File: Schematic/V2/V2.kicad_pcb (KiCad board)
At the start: 2 copper layers, 67 x 55 mm, 15 parts, among them J1 OUT1, J2 OUT2, J3 OUT3, J4 OUT4, J5 OUT5, J6 5V ESP, J7 5V LEDS

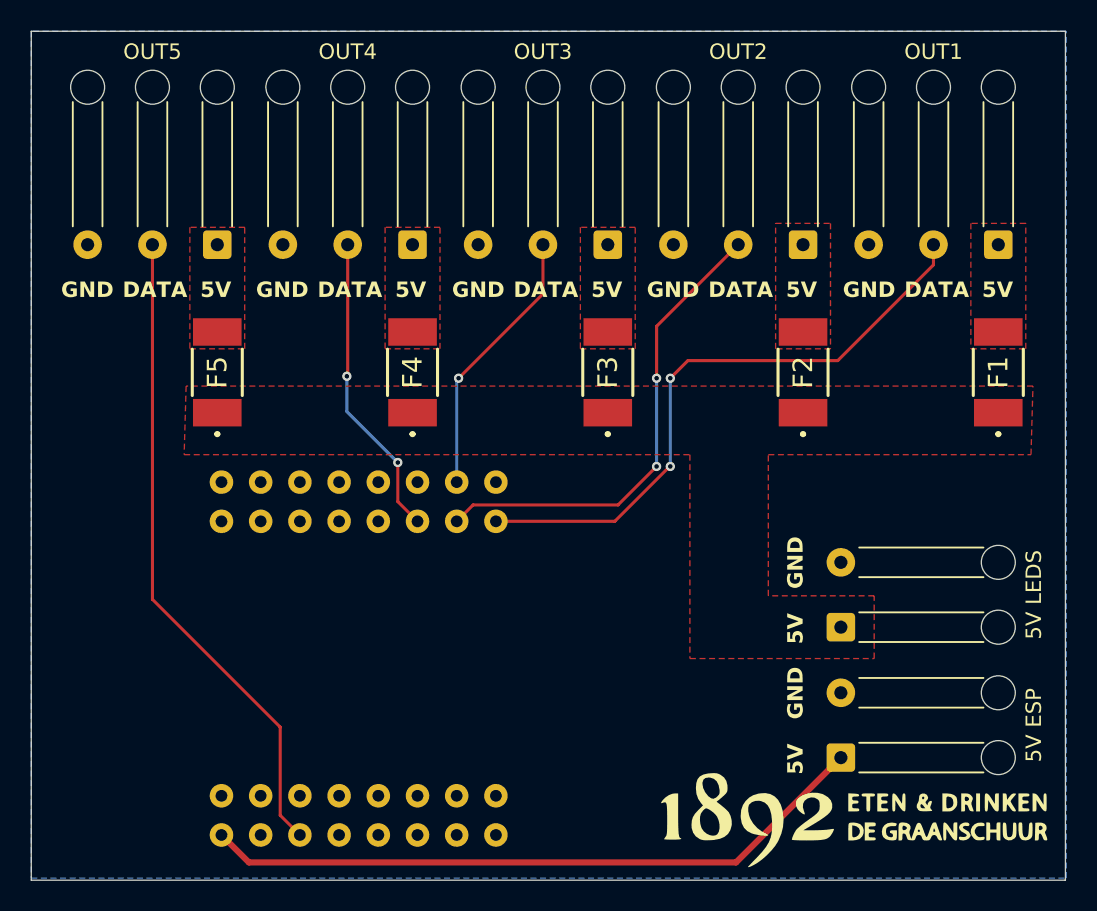
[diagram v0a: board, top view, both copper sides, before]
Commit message: Added support for two 18 AWG wires as 5V input to allow 14A and updated traces as needed.
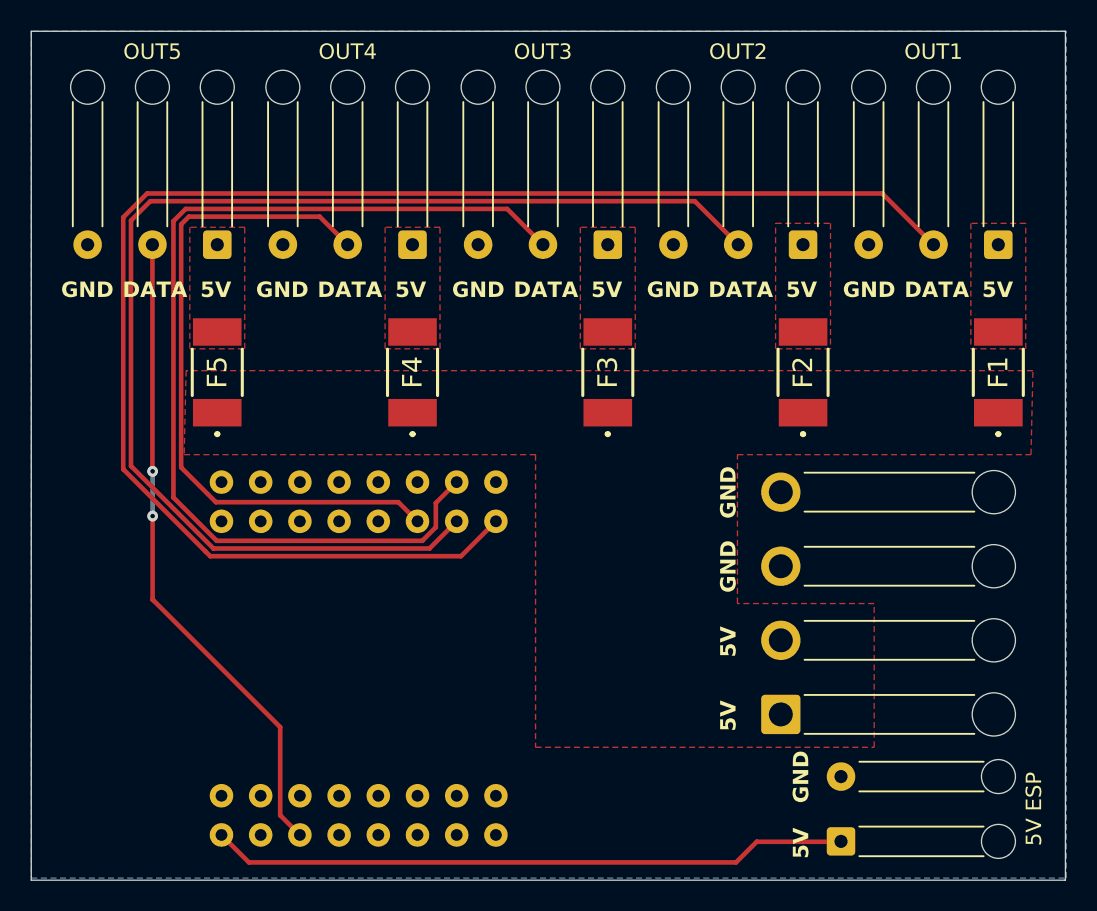
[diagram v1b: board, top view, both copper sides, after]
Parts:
- removed the G*** at (71.6, 66.3)
- J7: footprint Connector_Wire:SolderWire-0.25sqmm_1x02_P4.2mm_D0.65mm_OD1.7mm_Relief -> Connector_Wire:SolderWire-0.75sqmm_1x04_P4.8mm_D1.25mm_OD2.3mm_Relief
- moved J7 6.86 mm to (66.8, 59.5)
- moved J6 5.43 mm to (70.8, 67.7)
- moved G*** 2.20 mm to (49.2, 37.9)
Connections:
- J7 pad 2: GND -> +5V2
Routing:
- net OUT1: track 39.9 -> 98.2 mm, vias 2 -> 0
- net OUT2: track 31.0 -> 81.0 mm, vias 2 -> 0
- net OUT3: track 17.7 -> 65.1 mm, vias 1 -> 0
- net OUT4: track 19.8 -> 44.3 mm, vias 2 -> 0
- net +5V1: track 43.7 -> 41.4 mm
- net OUT5: vias 0 -> 2
